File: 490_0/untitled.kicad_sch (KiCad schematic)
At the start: 30 parts, among them J2 BM04B-PASS-1-TFT, J3 BM04B-PASS-1-TFT, U4 USB2512B-I/M2, Y1 24 MHz

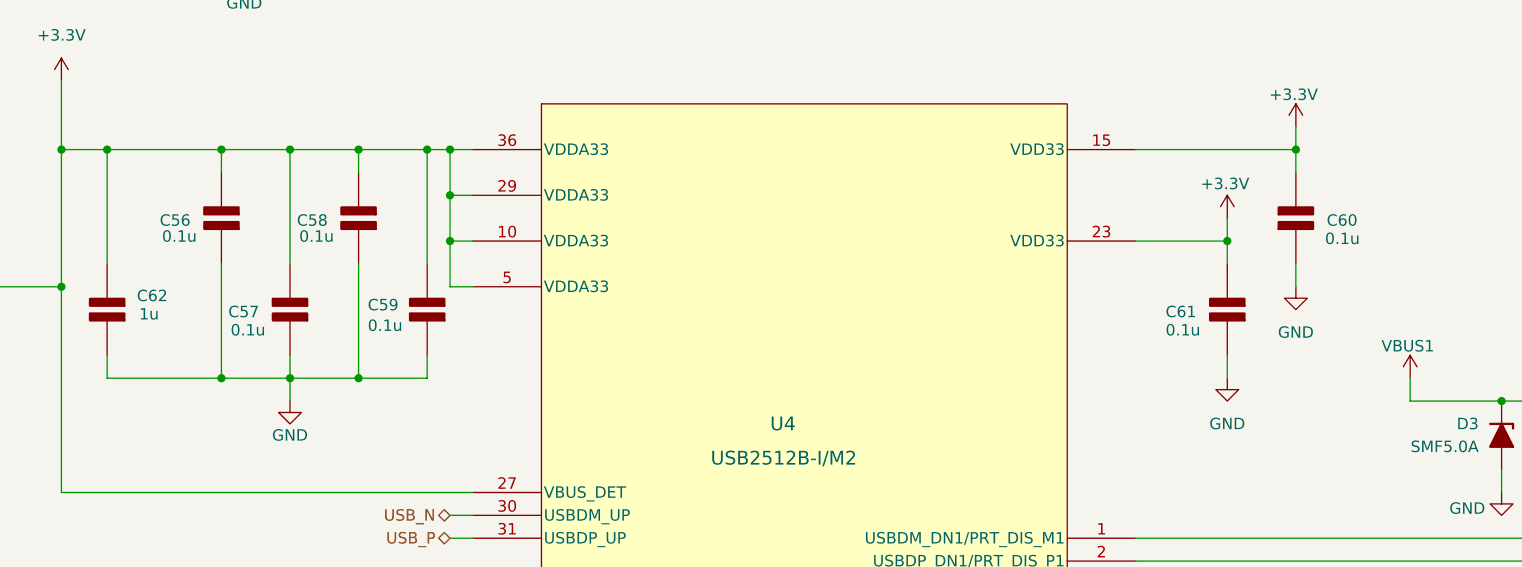
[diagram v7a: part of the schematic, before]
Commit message: Reviewed BOM
- changed some capacitors to a more fitting voltage rating
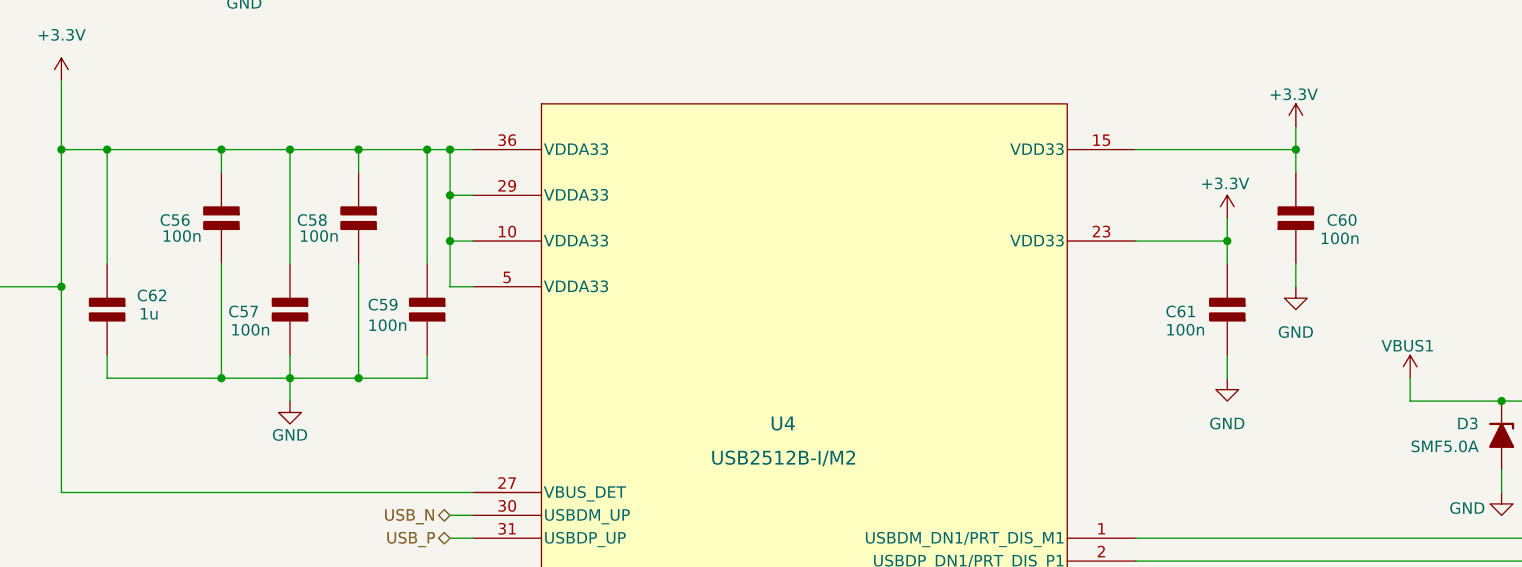
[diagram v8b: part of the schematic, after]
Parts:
- C53, C54: Digikey Link https://www.digikey.ca/en/products/detail/samsung-electro-m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 -> https://www.digikey.ca/en/products/detail/yageo/CC0805KRX7R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; Manufacturer Samsung Electro-Mechanics -> YAGEO; Manufacturer Part CL21B104KBCNNNC -> CC0805KRX7R9BB104; Package 0805 -> 0805 (2012 Metric); Supplier P/N 1276-1003-1-ND -> 311-1140-1-ND
- C56, C57, C58, C59, C60, C61: value 0.1u -> 100n; Digikey Link https://www.digikey.ca/en/products/detail/yageo/CC0805JRX7R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 -> https://www.digikey.ca/en/products/detail/yageo/CC0805KRX7R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; Manufacturer Part CC0805JRX7R7BB104 -> CC0805KRX7R9BB104; Package 0805 -> 0805 (2012 Metric); Price 0.11 -> 0.08; Supplier P/N 311-4266-1-ND -> 311-1140-1-ND
- C62: Digikey Link https://www.digikey.ca/en/products/detail/yageo/CC0805JKX7R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 -> https://www.digikey.ca/en/products/detail/samsung-electro-m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; Manufacturer YAGEO -> Samsung Electro-Mechanics; Manufacturer Part CC0805JKX7R8BB105 -> CL21B105KAFNNNE; Price 0.13 -> 0.08; Supplier P/N 13-CC0805JKX7R8BB105CT-ND -> 1276-1066-1-ND
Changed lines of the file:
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@@
 			)
 		)
-		(property "Value" "0.1u"
+		(property "Value" "100n"
 			(at 170.942 91.186 0)
 			(effects
@@
 			)
 		)
-		(property "Description" "CAP CER 0.1UF 16V X7R 0805"
+		(property "Description" "CAP CER 0.1UF 50V X7R 0805"
 			(at 177.8 88.9 0)
 			(effects
@@
 			)
 		)
-		(property "Digikey Link" "https://www.digikey.ca/en/products/detail/yageo/CC0805JRX7R7BB104/5884101"
+		(property "Digikey Link" "https://www.digikey.ca/en/products/detail/yageo/CC0805KRX7R9BB104/302874?s=N4IgTCBcDaIMJwAwA5EFYDSAlAGgdiwE4AhYgRkQBYQBdAXyA"
 			(at 177.8 88.9 0)
 			(effects
@@
 			)
 		)
-		(property "Manufacturer Part" "CC0805JRX7R7BB104"
+		(property "Manufacturer Part" "CC0805KRX7R9BB104"
 			(at 177.8 88.9 0)
 			(effects
@@
 			)
 		)
-		(property "Package" "0805"
+		(property "Package" "0805 (2012 Metric)"
 			(at 177.8 88.9 0)
 			(effects
@@
 			)
 		)
-		(property "Price" "0.11"
+		(property "Price" "0.08"
 			(at 177.8 88.9 0)
 			(effects
@@
 			)
 		)
-		(property "Supplier P/N" "311-4266-1-ND"
+		(property "Supplier P/N" "311-1140-1-ND"
 			(at 177.8 88.9 0)
 			(effects
@@
 			)
 		)
-		(property "Value" "0.1u"
+		(property "Value" "100n"
 			(at 82.296 90.678 0)
 			(effects
@@
 			)
 		)
-		(property "Description" "CAP CER 0.1UF 16V X7R 0805"
+		(property "Description" "CAP CER 0.1UF 50V X7R 0805"
 			(at 88.9 88.9 0)
 			(effects
@@
 			)
 		)
-		(property "Digikey Link" "https://www.digikey.ca/en/products/detail/yageo/CC0805JRX7R7BB104/5884101"
+		(property "Digikey Link" "https://www.digikey.ca/en/products/detail/yageo/CC0805KRX7R9BB104/302874?s=N4IgTCBcDaIMJwAwA5EFYDSAlAGgdiwE4AhYgRkQBYQBdAXyA"
 			(at 88.9 88.9 0)
 			(effects
@@
 			)
 		)
-		(property "Manufacturer Part" "CC0805JRX7R7BB104"
+		(property "Manufacturer Part" "CC0805KRX7R9BB104"
 			(at 88.9 88.9 0)
 			(effects
@@
 			)
 		)
-		(property "Package" "0805"
+		(property "Package" "0805 (2012 Metric)"
 			(at 88.9 88.9 0)
 			(effects
@@
 			)
 		)
-		(property "Price" "0.11"
+		(property "Price" "0.08"
 			(at 88.9 88.9 0)
 			(effects
@@
 			)
 		)
-		(property "Supplier P/N" "311-4266-1-ND"
+		(property "Supplier P/N" "311-1140-1-ND"
 			(at 88.9 88.9 0)
 			(effects
@@
 			)
 		)
-		(property "Datasheet" "kicad-embed://UPY-GPHC_X7R_6_3V-TO-250V.pdf"
+		(property "Datasheet" "kicad-embed://CL21B105KAFNNNE_Spec.pdf"
 			(at 53.34 88.9 0)
 			(effects
@@
 			)
 		)
-		(property "Description" "CAP CER 1UF 25V X7R 0805"
+		(property "Description" "1 µF ±10% 25V Ceramic Capacitor X7R 0805 (2012 Metric)"
 			(at 53.34 88.9 0)
 			(effects
@@
 			)
 		)
-		(property "Digikey Link" "https://www.digikey.ca/en/products/detail/yageo/CC0805JKX7R8BB105/16797938"
+		(property "Digikey Link" "https://www.digikey.ca/en/products/detail/samsung-electro-mechanics/CL21B105KAFNNNE/3886724"
 			(at 53.34 88.9 0)
 			(effects
@@
 			)
 		)
-		(property "Manufacturer" "YAGEO"
+		(property "Manufacturer" "Samsung Electro-Mechanics"
 			(at 53.34 88.9 0)
 			(effects
@@
 			)
 		)
-		(property "Manufacturer Part" "CC0805JKX7R8BB105"
+		(property "Manufacturer Part" "CL21B105KAFNNNE"
 			(at 53.34 88.9 0)
 			(effects
@@
 			)
 		)
-		(property "Price" "0.13"
+		(property "Price" "0.08"
 			(at 53.34 88.9 0)
 			(effects
@@
 			)
 		)
-		(property "Supplier P/N" "13-CC0805JKX7R8BB105CT-ND"
+		(property "Supplier P/N" "1276-1066-1-ND"
 			(at 53.34 88.9 0)
 			(effects
@@
 			)
 		)
-		(property "Datasheet" "kicad-embed://CL21B104KBCNNN_Spec.pdf"
+		(property "Datasheet" "kicad-embed://UPY-GPHC_X7R_6_3V-TO-250V.pdf"
 			(at 81.28 142.24 0)
 			(effects
@@
 			)
 		)
-		(property "Digikey Link" "https://www.digikey.ca/en/products/detail/samsung-electro-mechanics/CL21B104KBCNNNC/3886661"
+		(property "Digikey Link" "https://www.digikey.ca/en/products/detail/yageo/CC0805KRX7R9BB104/302874?s=N4IgTCBcDaIMJwAwA5EFYDSAlAGgdiwE4AhYgRkQBYQBdAXyA"
 			(at 81.28 142.24 0)
 			(effects
@@
 			)
 		)
-		(property "Manufacturer" "Samsung Electro-Mechanics"
+		(property "Manufacturer" "YAGEO"
 			(at 81.28 142.24 0)
 			(effects
@@
 			)
 		)
-		(property "Manufacturer Part" "CL21B104KBCNNNC"
+		(property "Manufacturer Part" "CC0805KRX7R9BB104"
 			(at 81.28 142.24 0)
 			(effects
@@
 			)
 		)
-		(property "Supplier P/N" "1276-1003-1-ND"
+		(property "Supplier P/N" "311-1140-1-ND"
 			(at 81.28 142.24 0)
 			(effects
@@
 			)
 		)
-		(property "Package" "0805"
+		(property "Package" "0805 (2012 Metric)"
 			(at 81.28 142.24 90)
 			(effects
@@
 			)
 		)
-		(property "Value" "0.1u"
+		(property "Value" "100n"
 			(at 59.436 80.772 0)
 			(effects
@@
 			)
 		)
-		(property "Description" "CAP CER 0.1UF 16V X7R 0805"
+		(property "Description" "CAP CER 0.1UF 50V X7R 0805"
 			(at 66.04 78.74 0)
 			(effects
@@
 			)
 		)
-		(property "Digikey Link" "https://www.digikey.ca/en/products/detail/yageo/CC0805JRX7R7BB104/5884101"
+		(property "Digikey Link" "https://www.digikey.ca/en/products/detail/yageo/CC0805KRX7R9BB104/302874?s=N4IgTCBcDaIMJwAwA5EFYDSAlAGgdiwE4AhYgRkQBYQBdAXyA"
 			(at 66.04 78.74 0)
 			(effects
@@
 			)
 		)
-		(property "Manufacturer Part" "CC0805JRX7R7BB104"
+		(property "Manufacturer Part" "CC0805KRX7R9BB104"
 			(at 66.04 78.74 0)
 			(effects
@@
 			)
 		)
-		(property "Package" "0805"
+		(property "Package" "0805 (2012 Metric)"
 			(at 66.04 78.74 0)
 			(effects
@@
 			)
 		)
-		(property "Price" "0.11"
+		(property "Price" "0.08"
 			(at 66.04 78.74 0)
 			(effects
@@
 			)
 		)
-		(property "Supplier P/N" "311-4266-1-ND"
+		(property "Supplier P/N" "311-1140-1-ND"
 			(at 66.04 78.74 0)
 			(effects
@@
 			)
 		)
-		(property "Datasheet" "kicad-embed://CL21B104KBCNNN_Spec.pdf"
+		(property "Datasheet" "kicad-embed://UPY-GPHC_X7R_6_3V-TO-250V.pdf"
 			(at 81.28 137.16 0)
 			(effects
@@
 			)
 		)
-		(property "Digikey Link" "https://www.digikey.ca/en/products/detail/samsung-electro-mechanics/CL21B104KBCNNNC/3886661"
+		(property "Digikey Link" "https://www.digikey.ca/en/products/detail/yageo/CC0805KRX7R9BB104/302874?s=N4IgTCBcDaIMJwAwA5EFYDSAlAGgdiwE4AhYgRkQBYQBdAXyA"
 			(at 81.28 137.16 0)
 			(effects
@@
 			)
 		)
-		(property "Manufacturer" "Samsung Electro-Mechanics"
+		(property "Manufacturer" "YAGEO"
 			(at 81.28 137.16 0)
 			(effects
@@
 			)
 		)
-		(property "Manufacturer Part" "CL21B104KBCNNNC"
+		(property "Manufacturer Part" "CC0805KRX7R9BB104"
 			(at 81.28 137.16 0)
 			(effects
@@
 			)
 		)
-		(property "Supplier P/N" "1276-1003-1-ND"
+		(property "Supplier P/N" "311-1140-1-ND"
 			(at 81.28 137.16 0)
 			(effects
@@
 			)
 		)
-		(property "Package" "0805"
+		(property "Package" "0805 (2012 Metric)"
 			(at 81.28 137.16 90)
 			(effects
@@
 			)
 		)
-		(property "Value" "0.1u"
+		(property "Value" "100n"
 			(at 67.056 91.186 0)
 			(effects
@@
 			)
 		)
-		(property "Description" "CAP CER 0.1UF 16V X7R 0805"
+		(property "Description" "CAP CER 0.1UF 50V X7R 0805"
 			(at 73.66 88.9 0)
 			(effects
@@
 			)
 		)
-		(property "Digikey Link" "https://www.digikey.ca/en/products/detail/yageo/CC0805JRX7R7BB104/5884101"
+		(property "Digikey Link" "https://www.digikey.ca/en/products/detail/yageo/CC0805KRX7R9BB104/302874?s=N4IgTCBcDaIMJwAwA5EFYDSAlAGgdiwE4AhYgRkQBYQBdAXyA"
 			(at 73.66 88.9 0)
 			(effects
@@
 			)
 		)
-		(property "Manufacturer Part" "CC0805JRX7R7BB104"
+		(property "Manufacturer Part" "CC0805KRX7R9BB104"
 			(at 73.66 88.9 0)
 			(effects
@@
 			)
 		)
-		(property "Package" "0805"
+		(property "Package" "0805 (2012 Metric)"
 			(at 73.66 88.9 0)
 			(effects
@@
 			)
 		)
-		(property "Price" "0.11"
+		(property "Price" "0.08"
 			(at 73.66 88.9 0)
 			(effects
@@
 			)
 		)
-		(property "Supplier P/N" "311-4266-1-ND"
+		(property "Supplier P/N" "311-1140-1-ND"
 			(at 73.66 88.9 0)
 			(effects
@@
 			)
 		)
-		(property "Value" "0.1u"
+		(property "Value" "100n"
 			(at 192.532 81.026 0)
 			(effects
@@
 			)
 		)
-		(property "Description" "CAP CER 0.1UF 16V X7R 0805"
+		(property "Description" "CAP CER 0.1UF 50V X7R 0805"
 			(at 185.42 78.74 0)
 			(effects
@@
 			)
 		)
-		(property "Digikey Link" "https://www.digikey.ca/en/products/detail/yageo/CC0805JRX7R7BB104/5884101"
+		(property "Digikey Link" "https://www.digikey.ca/en/products/detail/yageo/CC0805KRX7R9BB104/302874?s=N4IgTCBcDaIMJwAwA5EFYDSAlAGgdiwE4AhYgRkQBYQBdAXyA"
 			(at 185.42 78.74 0)
 			(effects
@@
 			)
 		)
-		(property "Manufacturer Part" "CC0805JRX7R7BB104"
+		(property "Manufacturer Part" "CC0805KRX7R9BB104"
 			(at 185.42 78.74 0)
 			(effects
@@
 			)
 		)
-		(property "Package" "0805"
+		(property "Package" "0805 (2012 Metric)"
 			(at 185.42 78.74 0)
 			(effects
@@
 			)
 		)
-		(property "Price" "0.11"
+		(property "Price" "0.08"
 			(at 185.42 78.74 0)
 			(effects
@@
 			)
 		)
-		(property "Supplier P/N" "311-4266-1-ND"
+		(property "Supplier P/N" "311-1140-1-ND"
 			(at 185.42 78.74 0)
 			(effects
@@
 			)
 		)
-		(property "Value" "0.1u"
+		(property "Value" "100n"
 			(at 74.676 80.772 0)
 			(effects
@@
 			)
 		)
-		(property "Description" "CAP CER 0.1UF 16V X7R 0805"
+		(property "Description" "CAP CER 0.1UF 50V X7R 0805"
 			(at 81.28 78.74 0)
 			(effects
@@
 			)
 		)
-		(property "Digikey Link" "https://www.digikey.ca/en/products/detail/yageo/CC0805JRX7R7BB104/5884101"
+		(property "Digikey Link" "https://www.digikey.ca/en/products/detail/yageo/CC0805KRX7R9BB104/302874?s=N4IgTCBcDaIMJwAwA5EFYDSAlAGgdiwE4AhYgRkQBYQBdAXyA"
 			(at 81.28 78.74 0)
 			(effects
@@
 			)
 		)
-		(property "Manufacturer Part" "CC0805JRX7R7BB104"
+		(property "Manufacturer Part" "CC0805KRX7R9BB104"
 			(at 81.28 78.74 0)
 			(effects
@@
 			)
 		)
-		(property "Package" "0805"
+		(property "Package" "0805 (2012 Metric)"
 			(at 81.28 78.74 0)
 			(effects
@@
 			)
 		)
-		(property "Price" "0.11"
+		(property "Price" "0.08"
 			(at 81.28 78.74 0)
 			(effects
@@
 			)
 		)
-		(property "Supplier P/N" "311-4266-1-ND"
+		(property "Supplier P/N" "311-1140-1-ND"
 			(at 81.28 78.74 0)
 			(effects
